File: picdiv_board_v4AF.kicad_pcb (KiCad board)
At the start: 2 copper layers, 100 x 99.5 mm, 83 parts, among them J1 DC-Input, J10 PPS_B, J11 PPS_B, J2 MountingHole_M2.5, J3 MountingHole_M2.5, J4 TEST_1PPS, J5 Conn_01x06, J6 Sync, J7 Sync, J8 10MHz, J9 10MHz, SW1 SW_DIP_x03, U1 LT1963AxST-3.3, U2 LT1963AxST-3.3, U3 PIC12F675-xSN, U4 LTC6993xS6-1, U5 IDT5PB1108, U6 IDT5PB1108, U7 LT1963AEQ, U8 ADR4540

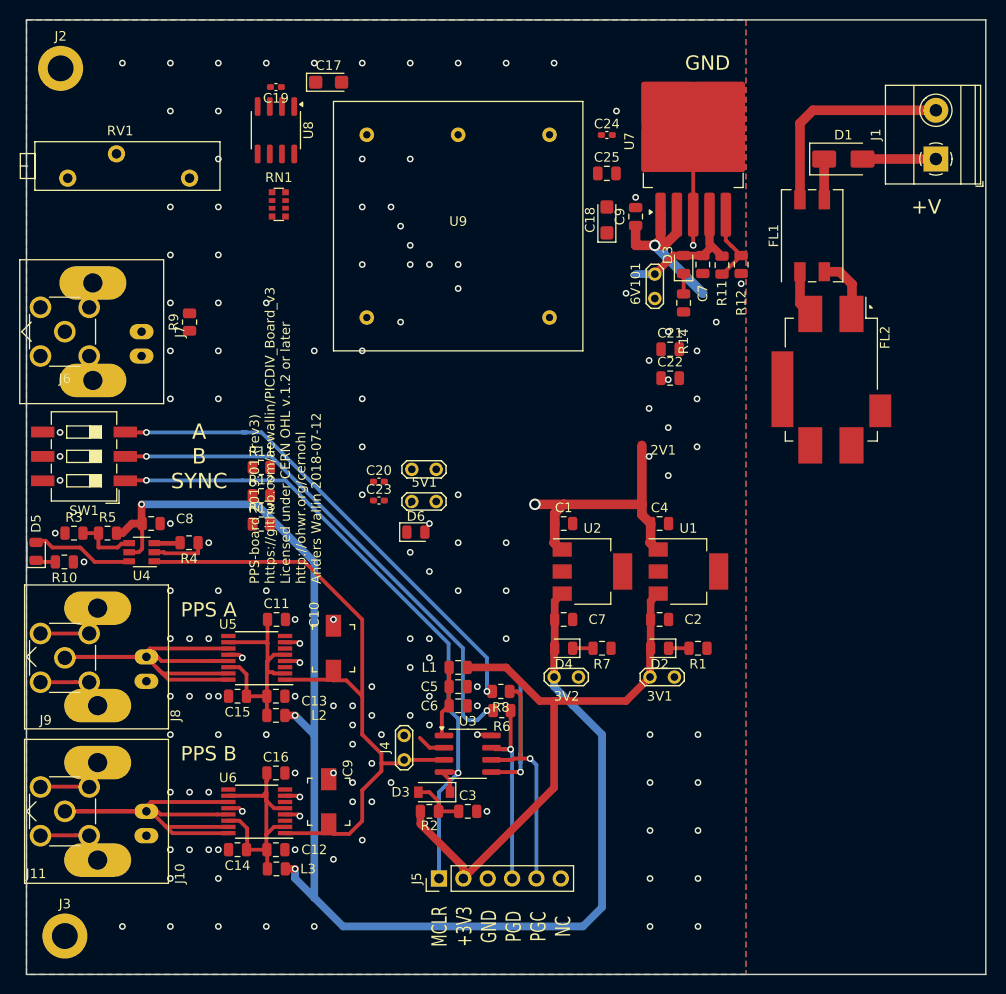
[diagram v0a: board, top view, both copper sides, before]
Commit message: Add 3D models
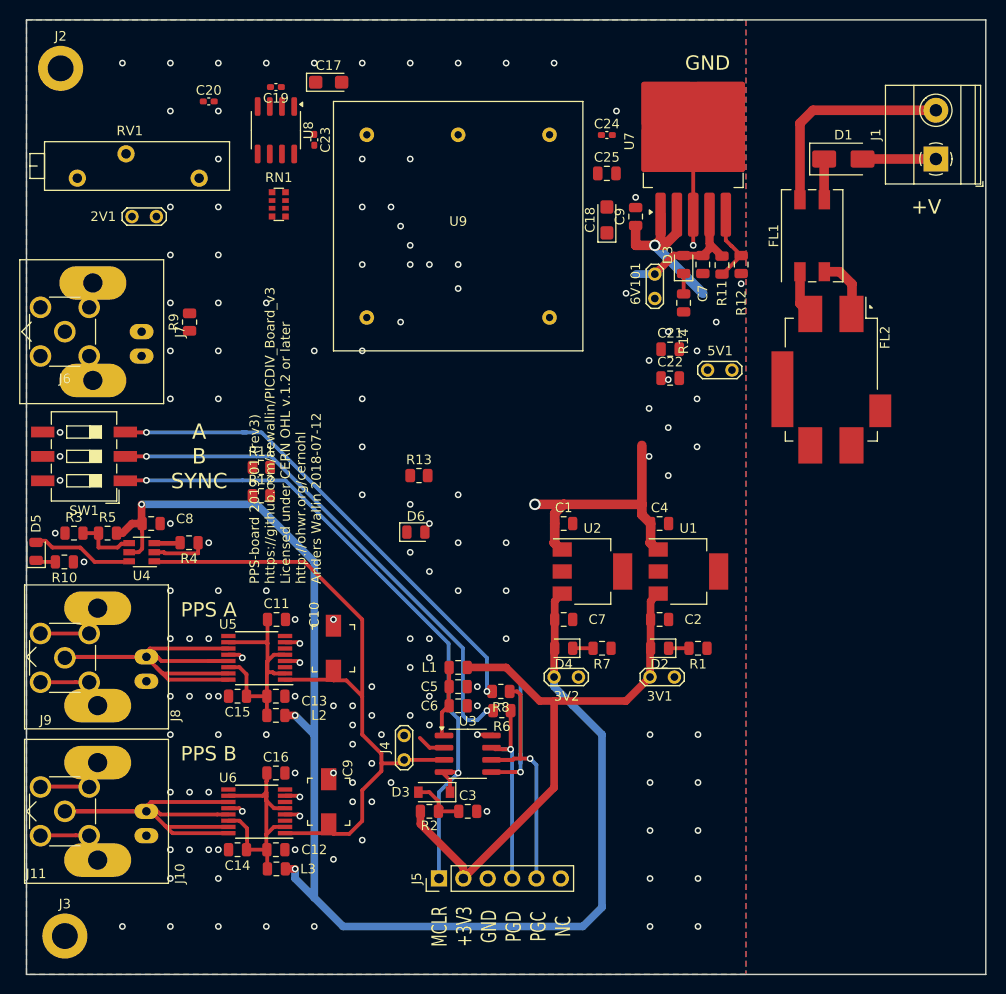
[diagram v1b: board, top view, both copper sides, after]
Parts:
- moved C20 43.4 mm to (144.0, 59.0)
- moved 2V1 39.3 mm to (136.0, 71.0)
- moved C23 38.2 mm to (155.0, 63.0), turned to -90 degrees
- moved 5V1 33.7 mm to (196.0, 87.0)
- moved R13 17.2 mm to (165.9, 98.0)
- moved RV1 1.00 mm to (143.0, 67.0)
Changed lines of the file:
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@@
 			)
 		)
+		(model "${KIPRJMOD}/3D-models/0732512200.stp"
+			(offset
+				(xyz 0 13.5 6)
+			)
+			(scale
+				(xyz 1 1 1)
+			)
+			(rotate
+				(xyz -90 0 90)
+			)
+		)
 	)
 	(footprint "Connector_Coaxial:SMA_Molex_73251-2200_Horizontal"
@@
 			)
 		)
+		(model "${KIPRJMOD}/3D-models/0732512200.stp"
+			(offset
+				(xyz 0 13.5 6)
+			)
+			(scale
+				(xyz 1 1 1)
+			)
+			(rotate
+				(xyz -90 0 90)
+			)
+		)
 	)
 	(footprint "Connector_Coaxial:BNC_Amphenol_B6252HB-NPP3G-50_Horizontal"
@@
 		)
 		(property "Value" "BNX025"
-			(at -1.9 7.75 -90)
+			(at -1.9 7.75 90)
 			(layer "F.Fab")
 			(effects
@@
 		)
 		(fp_text user "${REFERENCE}"
-			(at 0.75 0 -90)
+			(at 0.75 0 90)
 			(layer "F.Fab")
 			(effects
@@
 			)
 		)
+		(model "${KIPRJMOD}/3D-models/BNX025H01--3DModel-STEP-1.STEP"
+			(hide yes)
+			(offset
+				(xyz 0 0 0)
+			)
+			(scale
+				(xyz 1 1 1)
+			)
+			(rotate
+				(xyz 0 0 0)
+			)
+		)
 	)
 	(footprint "Connector_Coaxial:BNC_Amphenol_B6252HB-NPP3G-50_Horizontal"
@@
 	(footprint "TestPoint:TestPoint_2Pads_Pitch2.54mm_Drill0.8mm"
 		(layer "F.Cu")
-		(at 165.17 97.35)
+		(at 136 71)
 		(descr "Test point with 2 pins, pitch 2.54mm, drill diameter 0.8mm")
 		(tags "CONN DEV")
 		(property "Reference" "2V1"
-			(at 26.2 -2 0)
+			(at -3 0 0)
 			(layer "F.SilkS")
 			(effects
@@
 			)
 		)
+		(model "${KIPRJMOD}/3D-models/0732512200.stp"
+			(offset
+				(xyz 0 13.5 6)
+			)
+			(scale
+				(xyz 1 1 1)
+			)
+			(rotate
+				(xyz -90 0 90)
+			)
+		)
 	)
 	(footprint "Resistor_SMD:R_0805_2012Metric"
@@
 	(footprint "TestPoint:TestPoint_2Pads_Pitch2.54mm_Drill0.8mm"
 		(layer "F.Cu")
-		(at 165.17 100.7)
+		(at 196 87)
 		(descr "Test point with 2 pins, pitch 2.54mm, drill diameter 0.8mm")
 		(tags "CONN DEV")
@@
 			)
 		)
-		(property "Description" "2.15kΩ ±25ppm/℃ ±0.1%"
+		(property "Description" "2.15kÎ© Â±25ppm/â Â±0.1%"
 			(at 0 0 0)
 			(unlocked yes)
@@
 	(footprint "Resistor_SMD:R_0805_2012Metric"
 		(layer "F.Cu")
-		(at 149.48 103.05)
+		(at 165.9125 98)
 		(descr "Resistor SMD 0805 (2012 Metric), square (rectangular) end terminal, IPC_7351 nominal, (Body size source: IPC-SM-782 page 72, https://www.pcb-3d.com/wordpress/wp-content/uploads/ipc-sm-782a_amendment_1_and_2.pdf), generated with kicad-footprint-generator")
 		(tags "resistor")
@@
 	(footprint "Capacitor_SMD:C_0402_1005Metric_Pad0.74x0.62mm_HandSolder"
 		(layer "F.Cu")
-		(at 161.74 100.6)
+		(at 155 63 -90)
 		(descr "Capacitor SMD 0402 (1005 Metric), square (rectangular) end terminal, IPC_7351 nominal with elongated pad for handsoldering. (Body size source: IPC-SM-782 page 76, https://www.pcb-3d.com/wordpress/wp-content/uploads/ipc-sm-782a_amendment_1_and_2.pdf), generated with kicad-footprint-generator")
 		(tags "capacitor handsolder")
 		(property "Reference" "C23"
-			(at 0 -1.16 0)
+			(at 0 -1.16 90)
 			(layer "F.SilkS")
 			(effects
@@
 		)
 		(property "Value" "100nF"
-			(at 0 1.16 0)
+			(at 0 1.16 90)
 			(layer "F.Fab")
 			(effects
@@
 		)
 		(property "Footprint" "Capacitor_SMD:C_0402_1005Metric_Pad0.74x0.62mm_HandSolder"
-			(at 0 0 0)
+			(at 0 0 -90)
 			(unlocked yes)
 			(layer "F.Fab")
@@
 		)
 		(property "Datasheet" ""
-			(at 0 0 0)
+			(at 0 0 -90)
 			(unlocked yes)
 			(layer "F.Fab")
@@
 		)
 		(property "Description" "Unpolarized capacitor"
-			(at 0 0 0)
+			(at 0 0 -90)
 			(unlocked yes)
 			(layer "F.Fab")
@@
 		)
 		(property "LCSC" "C1525"
-			(at 0 0 0)
+			(at 0 0 -90)
 			(unlocked yes)
 			(layer "F.Fab")
@@
 		)
 		(property "MPN" "CL05B104KO5NNNC "
-			(at 0 0 0)
+			(at 0 0 -90)
 			(unlocked yes)
 			(layer "F.Fab")
@@
 		(attr smd)
 		(fp_line
-			(start -0.115835 -0.36)
-			(end 0.115835 -0.36)
+			(start -0.115835 0.36)
+			(end 0.115835 0.36)
 			(stroke
 				(width 0.12)
@@
 		)
 		(fp_line
-			(start -0.115835 0.36)
-			(end 0.115835 0.36)
+			(start -0.115835 -0.36)
+			(end 0.115835 -0.36)
 			(stroke
 				(width 0.12)
@@
 		)
 		(fp_line
-			(start -1.08 -0.46)
-			(end 1.08 -0.46)
+			(start -1.08 0.46)
+			(end -1.08 -0.46)
 			(stroke
 				(width 0.05)
@@
 		)
 		(fp_line
-			(start -1.08 0.46)
-			(end -1.08 -0.46)
+			(start 1.08 0.46)
+			(end -1.08 0.46)
 			(stroke
 				(width 0.05)
@@
 		)
 		(fp_line
-			(start 1.08 -0.46)
-			(end 1.08 0.46)
+			(start -1.08 -0.46)
+			(end 1.08 -0.46)
 			(stroke
 				(width 0.05)
@@
 		)
 		(fp_line
-			(start 1.08 0.46)
-			(end -1.08 0.46)
+			(start 1.08 -0.46)
+			(end 1.08 0.46)
 			(stroke
 				(width 0.05)
@@
 		)
 		(fp_line
-			(start -0.5 -0.25)
-			(end 0.5 -0.25)
+			(start -0.5 0.25)
+			(end -0.5 -0.25)
 			(stroke
 				(width 0.1)
@@
 		)
 		(fp_line
-			(start -0.5 0.25)
-			(end -0.5 -0.25)
+			(start 0.5 0.25)
+			(end -0.5 0.25)
 			(stroke
 				(width 0.1)
@@
 		)
 		(fp_line
-			(start 0.5 -0.25)
-			(end 0.5 0.25)
+			(start -0.5 -0.25)
+			(end 0.5 -0.25)
 			(stroke
 				(width 0.1)
@@
 		)
 		(fp_line
-			(start 0.5 0.25)
-			(end -0.5 0.25)
+			(start 0.5 -0.25)
+			(end 0.5 0.25)
 			(stroke
 				(width 0.1)
@@
 		)
 		(fp_text user "${REFERENCE}"
-			(at 0 0 0)
+			(at 0 0 90)
 			(layer "F.Fab")
 			(effects
@@
 		)
 		(pad "1" smd roundrect
-			(at -0.5675 0)
+			(at -0.5675 0 270)
 			(size 0.735 0.62)
 			(layers "F.Cu" "F.Paste" "F.Mask")
@@
 		)
 		(pad "2" smd roundrect
-			(at 0.5675 0)
+			(at 0.5675 0 270)
 			(size 0.735 0.62)
 			(layers "F.Cu" "F.Paste" "F.Mask")
@@
 	(footprint "Potentiometer_THT:Potentiometer_Bourns_3006P_Horizontal"
 		(layer "F.Cu")
-		(at 142 67)
+		(at 143 67)
 		(descr "Potentiometer, horizontal, Bourns 3006P, https://www.bourns.com/docs/Product-Datasheets/3006.pdf")
 		(tags "Potentiometer horizontal Bourns 3006P")
@@
 	(footprint "Capacitor_SMD:C_0402_1005Metric_Pad0.74x0.62mm_HandSolder"
 		(layer "F.Cu")
-		(at 161.74 98.63)
+		(at 144 59)
 		(descr "Capacitor SMD 0402 (1005 Metric), square (rectangular) end terminal, IPC_7351 nominal with elongated pad for handsoldering. (Body size source: IPC-SM-782 page 76, https://www.pcb-3d.com/wordpress/wp-content/uploads/ipc-sm-782a_amendment_1_and_2.pdf), generated with kicad-footprint-generator")
 		(tags "capacitor handsolder")
@@
 			(footprints allowed)
 		)
-		(fill yes
+		(fill
 			(thermal_gap 0.508)
 			(thermal_bridge_width 0.508)
@@
 			(footprints allowed)
 		)
-		(fill yes
+		(fill
 			(thermal_gap 0.508)
 			(thermal_bridge_width 0.508)

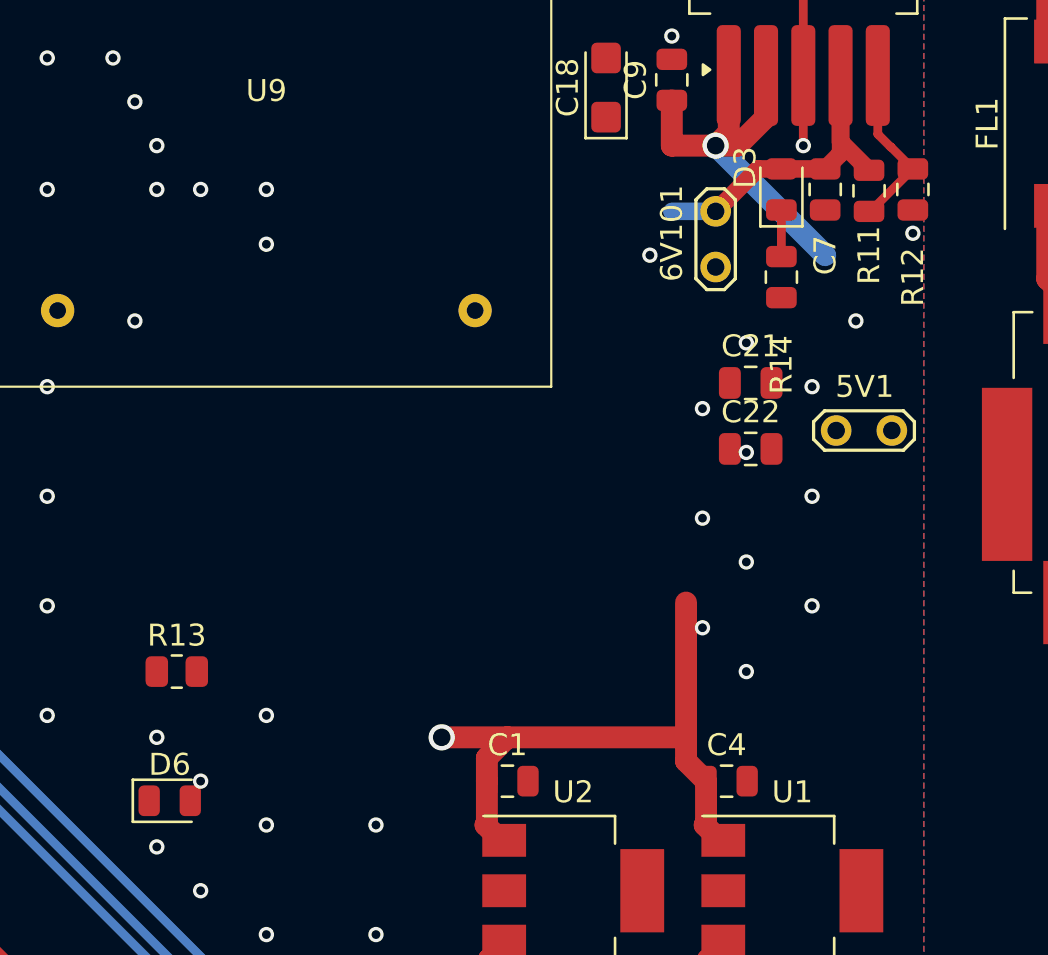
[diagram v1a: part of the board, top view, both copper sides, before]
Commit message: Fix more orphans
Fix parts resulting from change to 5V from 6V.
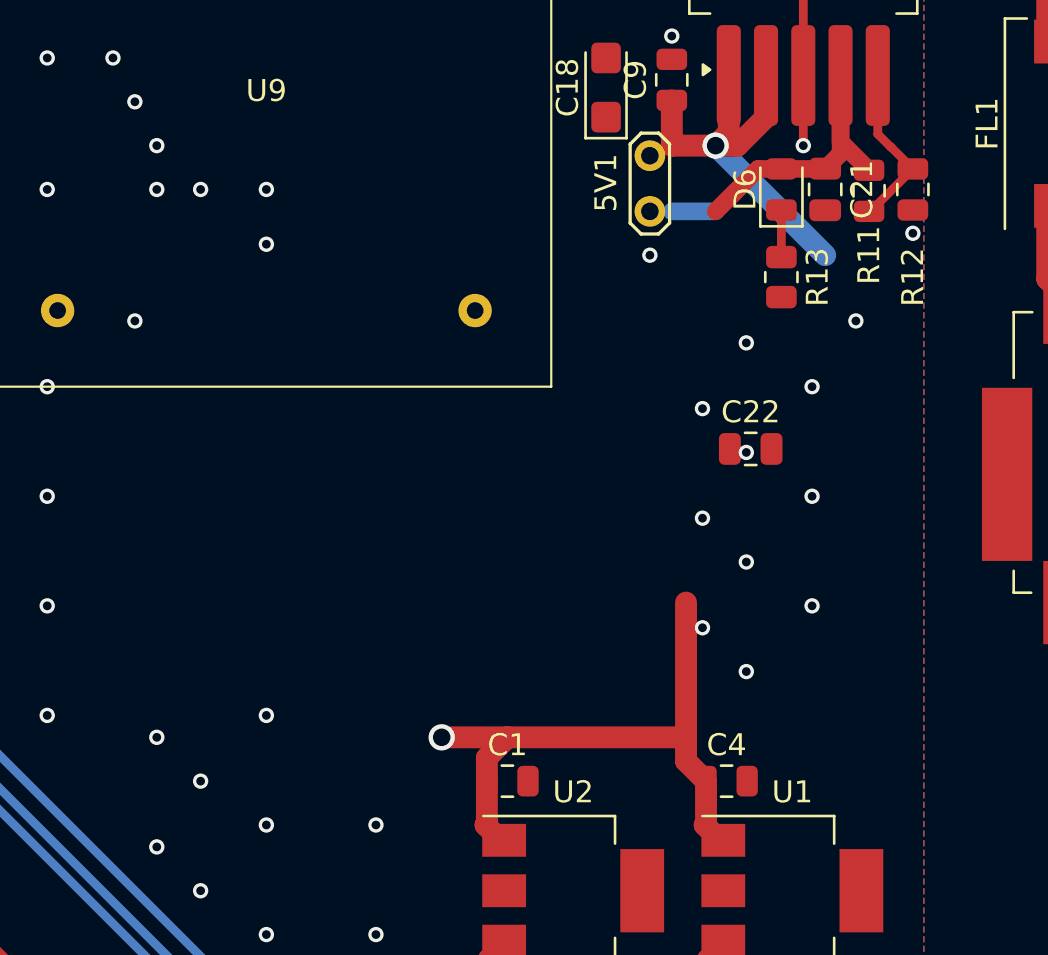
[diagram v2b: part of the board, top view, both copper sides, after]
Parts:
- removed 6V101: TEST_6V, TestPoint:TestPoint_2Pads_Pitch2.54mm_Drill0.8mm
- removed the C7 at (195.5, 76.0)
- removed the D3 at (193.5, 76.0)
- removed R14: 200R, Resistor_SMD:R_0805_2012Metric
- moved D6 39.5 mm to (193.5, 76.0), turned to 90 degrees
- moved R13 32.9 mm to (193.5, 80.0), turned to -90 degrees
- moved 5V1 13.1 mm to (187.5, 77.0), turned to 90 degrees
- moved C21 9.46 mm to (195.5, 76.0), turned to -90 degrees
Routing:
- net Net-(D6-K): track 0.00 -> 2.12 mm
- net Net-(D3-Pad1): track 2.12 -> 0.00 mm
- net +6V: track 17.3 -> 15.3 mm
- net +5V: track 0.00 -> 2.00 mm

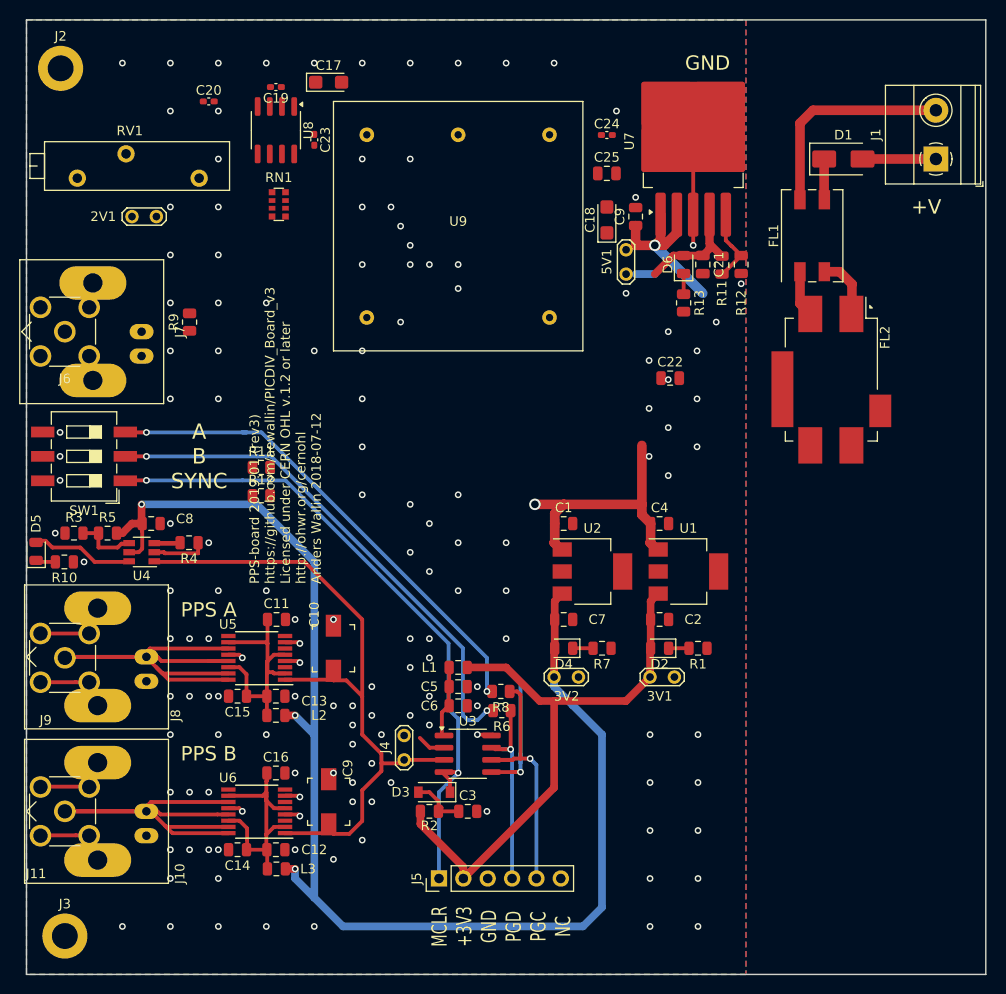
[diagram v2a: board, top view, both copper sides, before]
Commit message: DC Input layout
Fix keep out area around DC Input.   Add vias to FL2 GND.   The vias used to be in the foot print, but are no longer there in the current version of KiCad.  Easier to keep the library part and add the vias.
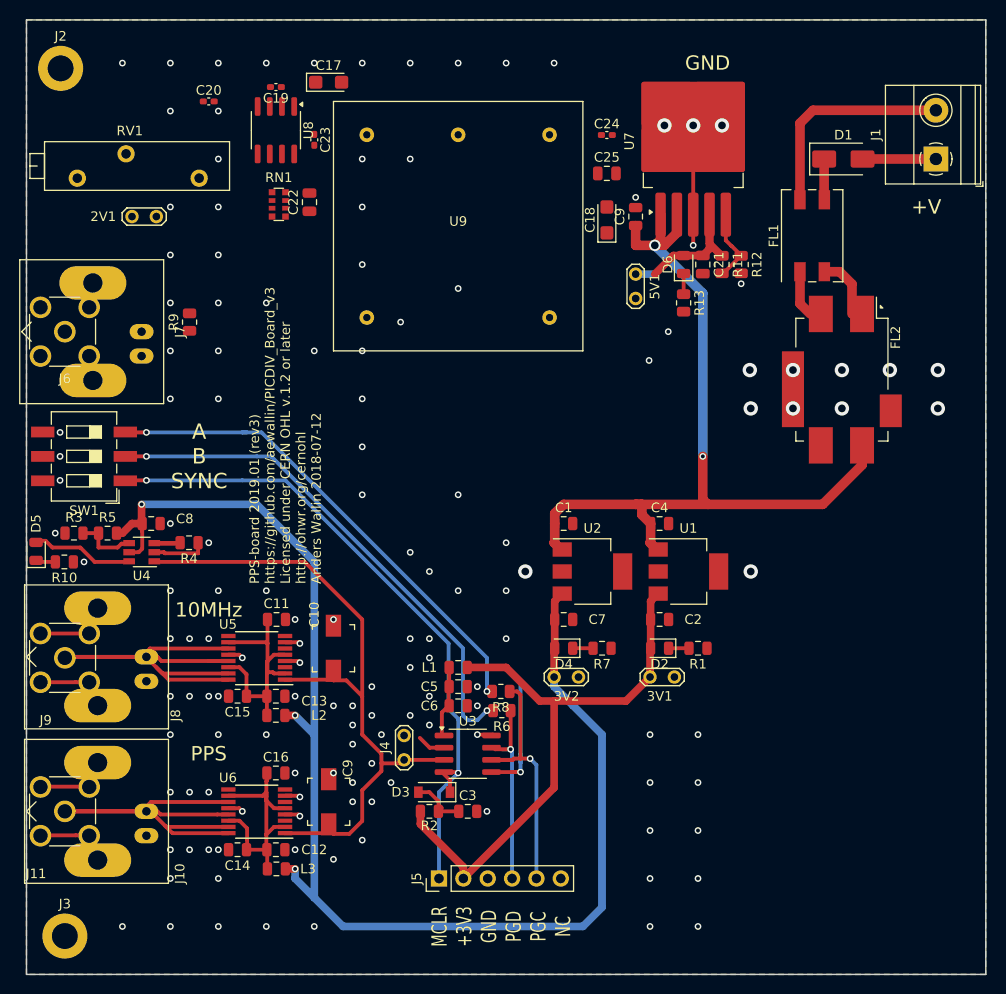
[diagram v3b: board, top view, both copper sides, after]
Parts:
- removed the R11 at (197.5, 76.1)
- removed the R12 at (199.5, 76.0)
- D3: value 1N4148 -> 1N4148W
- R1, R7: value 82R -> 100Ω
- R9: value 50R -> 50
- moved R12 55.5 mm to (199.5, 76.0), turned to -90 degrees
- moved R11 52.5 mm to (197.5, 76.0), turned to -90 degrees
- moved C22 41.8 mm to (154.5, 69.5), turned to 90 degrees
- moved FL2 1.10 mm to (210.0, 88.0)
- moved 5V1 1.00 mm to (188.5, 77.0), turned to -90 degrees
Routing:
- net LDO_IN: track 47.8 -> 88.2 mm, vias 3 -> 2
- net Net-(U7-ADJ): track 0.00 -> 7.76 mm
- net Net-(R11-Pad2): track 7.76 -> 0.00 mm
- net Net-(RN1-R1.2): vias 2 -> 0
- net +5V: vias 3 -> 0
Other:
- rule pad_to_mask_clearance: 0.2 -> 0
- board text added: "10MHz"
- board text added: "PPS"
- board text removed: "PPS A"
- board text removed: "PPS B"

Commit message: More layout
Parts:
- 5V1: value TEST_5V -> 5V
- moved C24 33.9 mm to (161.0, 86.0)
- moved C25 32.7 mm to (161.3, 88.5)
- turned C21 to 90 degrees
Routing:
- net +5V: track 2.00 -> 54.2 mm
- net +6V: track 15.3 -> 0.00 mm
- net LDO_IN: track 88.2 -> 91.7 mm
- net Net-(RN1-R2.2): vias 1 -> 0
- net GND: vias 141 -> 140
